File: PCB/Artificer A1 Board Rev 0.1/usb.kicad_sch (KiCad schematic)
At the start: 24 parts, among them U11 CH217K, U3 CH334F_C5187527, U5 CH217K, U6 GT-USB-7010ASV, X1 SMD-3225_4P12M12PF10PPM

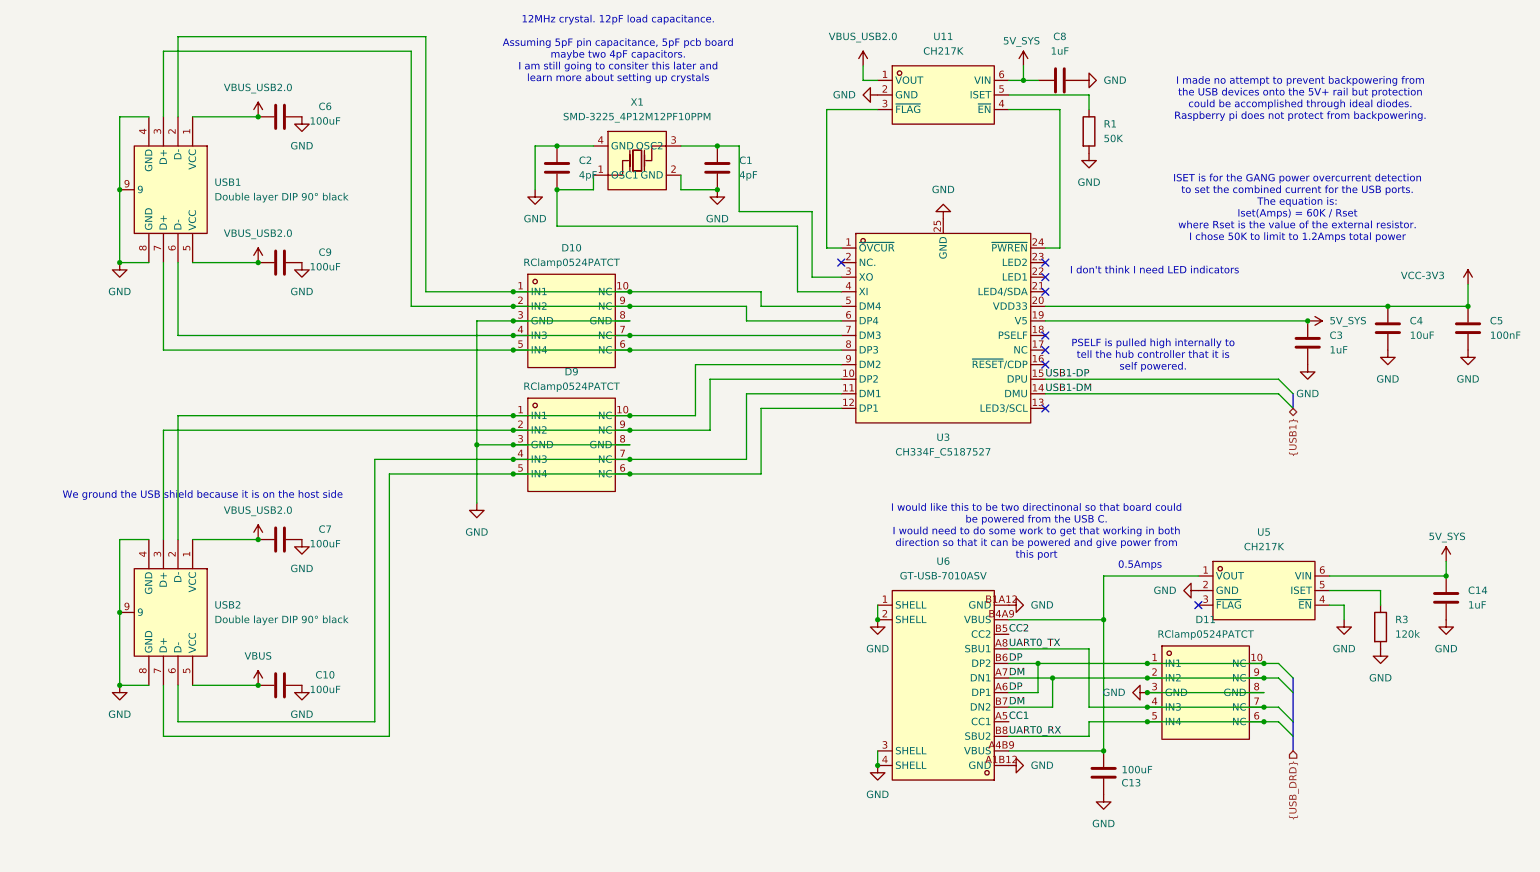
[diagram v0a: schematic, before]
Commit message: cleaned up, kicad 10 & usb c pd
migrated to Kicad 10,
added USB PD for power input
added capacitors inductors and resistor footprints
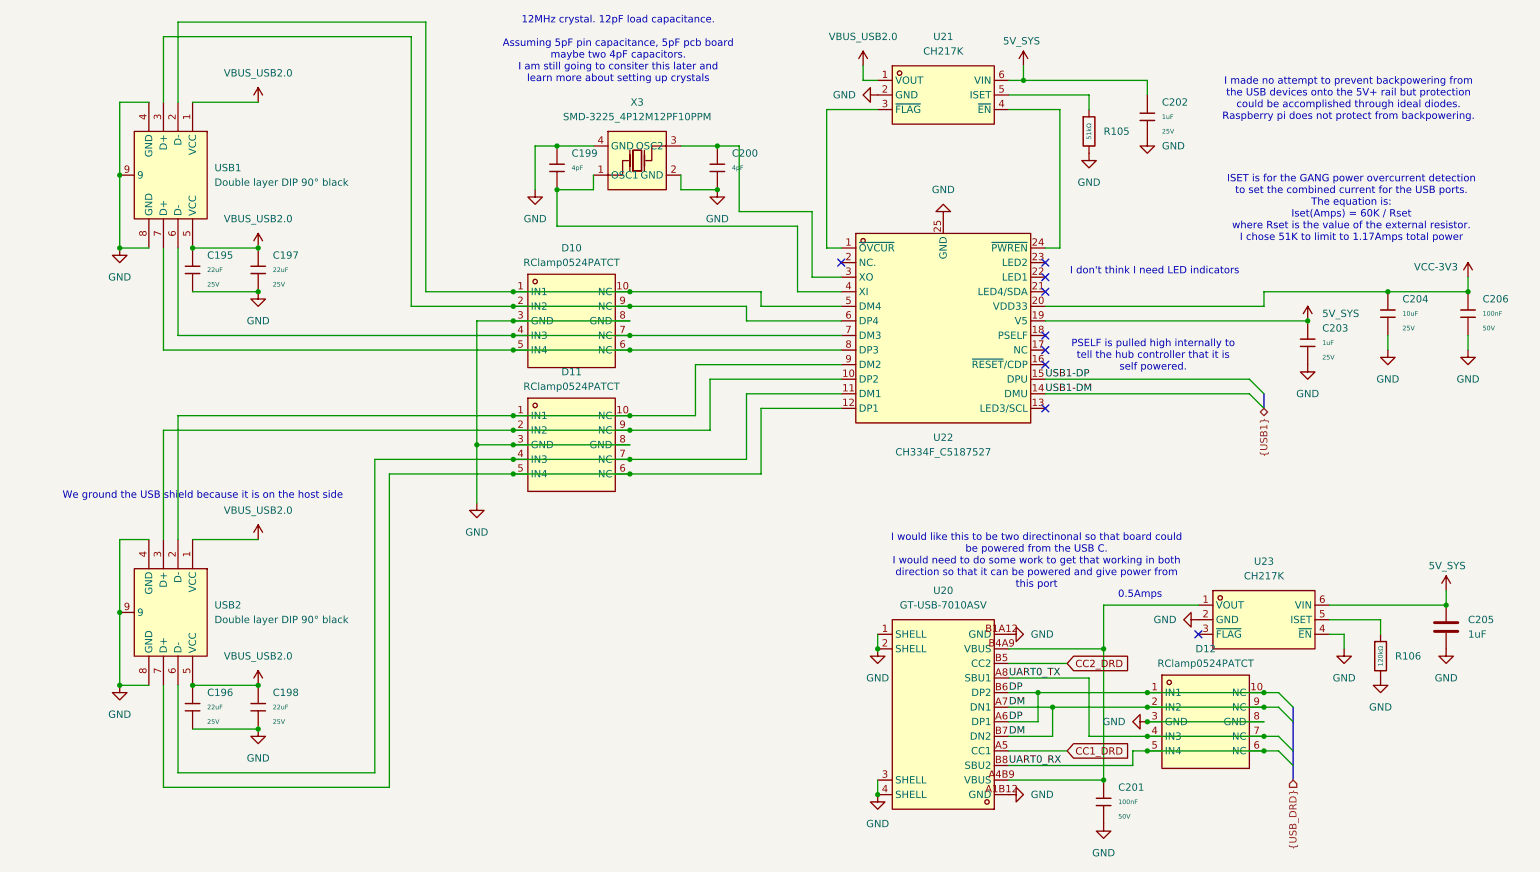
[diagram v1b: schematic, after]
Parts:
- removed C1, C2: 4pF, Capacitor_SMD:C_0201_0603Metric, symbol Device:C
- removed C10, C13, C6, C7, C9: 100uF, symbol Device:C
- removed C3, C8: 1uF, symbol Device:C
- removed C4: 10uF, symbol Device:C
- removed C5: 100nF, symbol Device:C
- removed R1: 50K, symbol Device:R
- removed R3: 120k, symbol Device:R
- added C195, C196, C197, C198: 22uF, PCM_JLCPCB:C_0805, symbol PCM_JLCPCB-Capacitors:0805,22uF
- added C199, C200: 4pF, PCM_JLCPCB:C_0402, symbol PCM_JLCPCB-Capacitors:0402,10pF
- added C201, C206: 100nF, PCM_JLCPCB:C_0402, symbol PCM_JLCPCB-Capacitors:0402,100nF,(2)
- added C202, C203: 1uF, PCM_JLCPCB:C_0402, symbol PCM_JLCPCB-Capacitors:0402,1uF
- added C204: 10uF, PCM_JLCPCB:C_0603, symbol PCM_JLCPCB-Capacitors:0603,10uF,(2)
- added R105: 51kΩ, PCM_JLCPCB:R_0402, symbol PCM_JLCPCB-Resistors:0402,51kΩ
- added R106: 120kΩ, PCM_JLCPCB:R_0402, symbol PCM_JLCPCB-Resistors:0402,120kΩ
- renumbered C14 to C205, D9 to D11, D11 to D12, U6 to U20, U11 to U21, U3 to U22, U5 to U23, X1 to X3
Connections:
- net VBUS is gone; now on net VBUS_USB2.0: USB2.5 (VCC)
- net 5V_SYS: now also C202.1, C203.1
- net GND: now also C195.2, C196.2, C197.2, C198.2, C199.1, C200.2, C201.2, C202.2, C203.2, C204.2, C206.2, R105.2, R106.2
- net VBUS_USB2.0: now also C195.1, C196.1, C197.1, C198.1
- net VCC-3V3: now also C204.1, C206.1
- net at U20.A4B9 (VBUS), U20.B4A9 (VBUS), U23.1 (VOUT): now also C201.1
- net at U22.3 (XO), X3.3 (OSC2): now also C200.1
- net at U22.4 (XI), X3.1 (OSC1): now also C199.2
- net at U23.5 (ISET): now also R106.1
- net at U21.5 (ISET): now also R105.1
- net CC1 renamed CC1_DRD
- net CC2 renamed CC2_DRD
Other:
- note added: "ISET is for the GANG power overcurrent detection to set the combined current for the USB ports. The equation is: Iset(Amps) = 60K / Rset where Rset is the value of the external resistor. I chose 51K to limit to 1.17Amps total power"
- note removed: "ISET is for the GANG power overcurrent detection to set the combined current for the USB ports. The equation is: Iset(Amps) = 60K / Rset where Rset is the value of the external resistor. I chose 50K to limit to 1.2Amps total power"
- moved on the sheet: C205, D12, U20, U23, USB1
